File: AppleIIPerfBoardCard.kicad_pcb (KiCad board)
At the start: 2 copper layers, 177.8 x 77.5 mm, 1770 parts, among them J1 Conn_02x25_Counter_Clockwise, J2 50_POS_Card_Edge_Connector

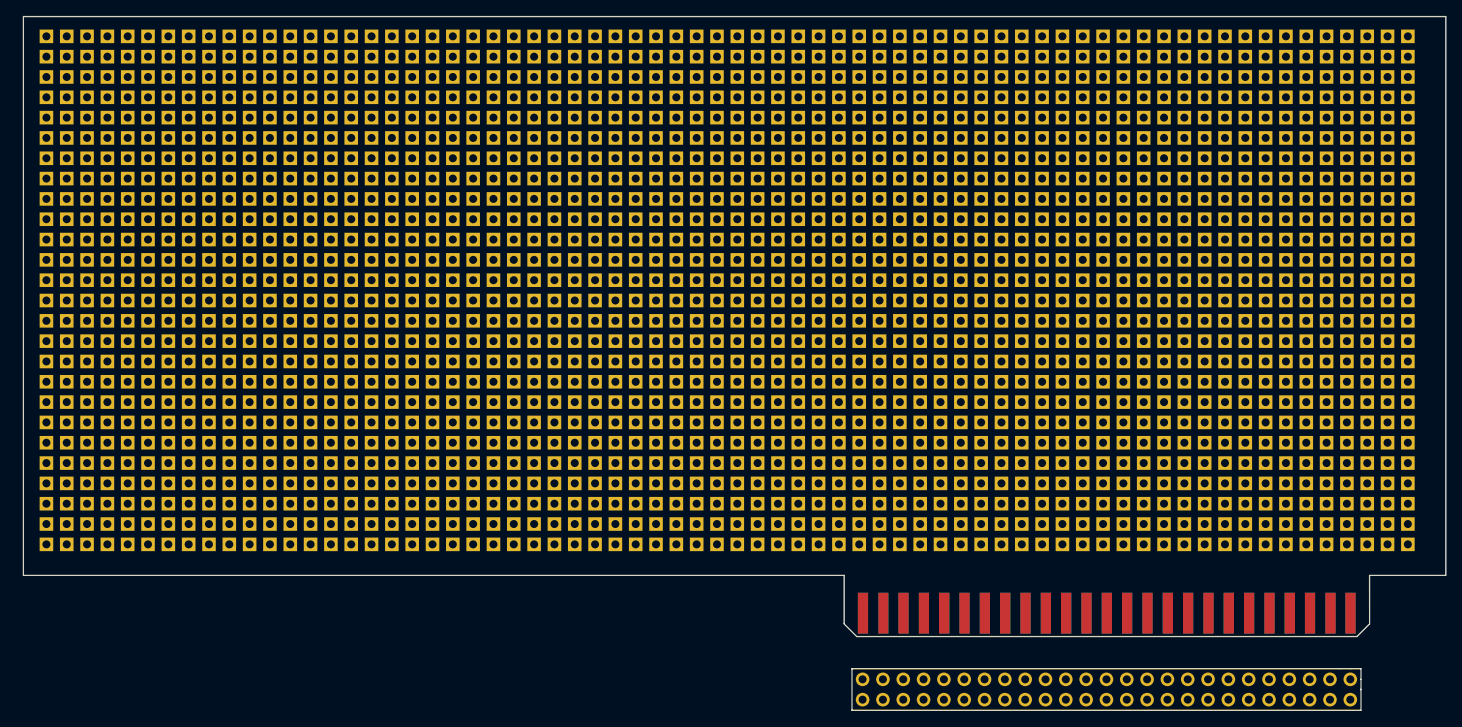
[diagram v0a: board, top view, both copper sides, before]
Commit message: refining perf board and edge connector position
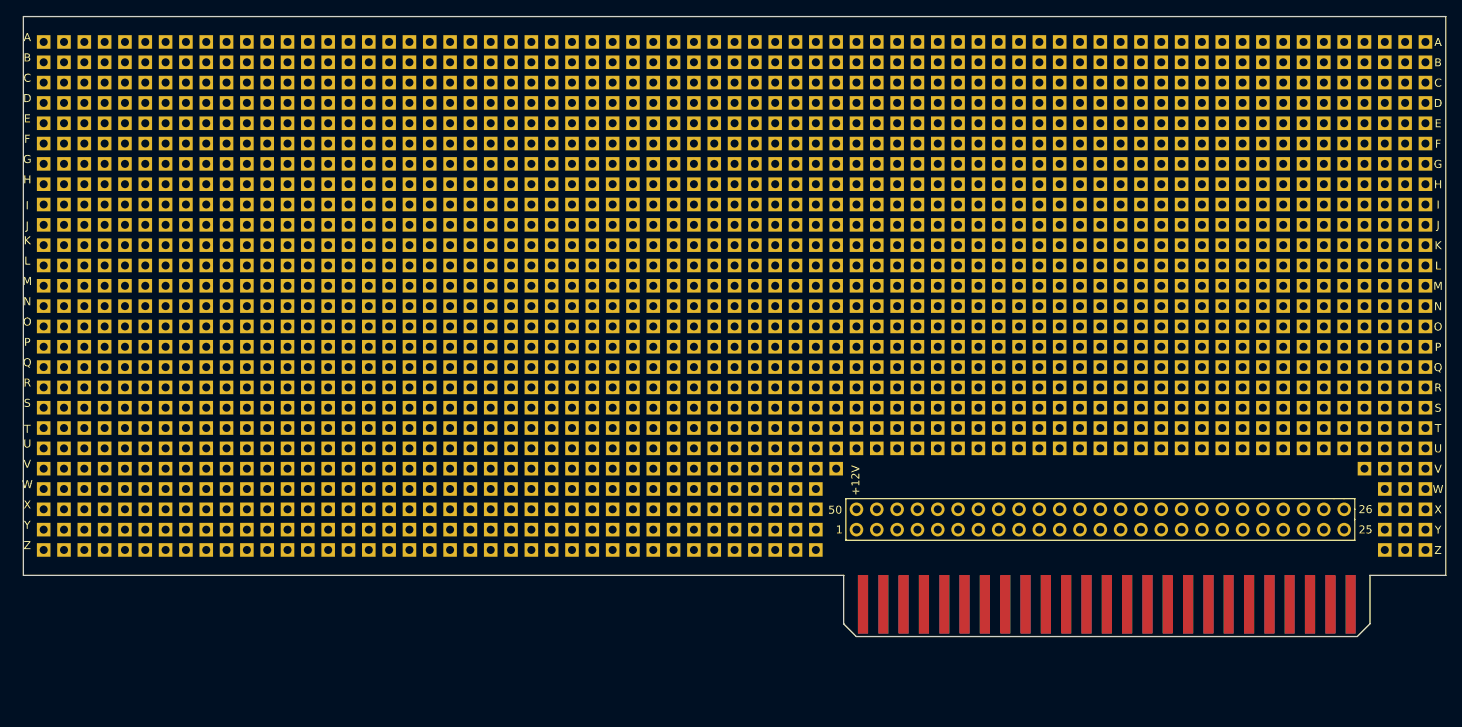
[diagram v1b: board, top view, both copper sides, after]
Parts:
- removed the REF** at (228.1, 126.3)
- removed the REF** at (205.2, 126.3)
- removed the REF** at (149.3, 123.7)
- removed the REF** at (108.7, 90.7)
- removed the REF** at (106.1, 90.7)
- removed the REF** at (103.6, 90.7)
- removed the REF** at (101.1, 90.7)
- removed the REF** at (98.5, 90.7)
- removed the REF** at (96.0, 90.7)
- removed the REF** at (93.4, 90.7)
- removed the REF** at (90.9, 90.7)
- removed the REF** at (88.4, 90.7)
- removed the REF** at (85.8, 90.7)
- removed the REF** at (146.8, 123.7)
- removed the REF** at (83.3, 90.7)
- removed the REF** at (80.7, 90.7)
- removed the REF** at (78.2, 90.7)
- removed the REF** at (75.7, 90.7)
- removed the REF** at (73.1, 90.7)
- removed the REF** at (70.6, 90.7)
- removed the REF** at (68.0, 90.7)
- removed the REF** at (65.5, 90.7)
- removed the REF** at (63.0, 90.7)
- removed the REF** at (60.4, 90.7)
- removed the REF** at (144.2, 123.7)
- removed the REF** at (57.9, 90.7)
- removed the REF** at (228.1, 88.2)
- removed the REF** at (225.5, 88.2)
- removed the REF** at (223.0, 88.2)
- removed the REF** at (220.4, 88.2)
- removed the REF** at (217.9, 88.2)
- removed the REF** at (215.4, 88.2)
- removed the REF** at (212.8, 88.2)
- removed the REF** at (210.3, 88.2)
- removed the REF** at (207.7, 88.2)
- removed the REF** at (141.7, 123.7)
- removed the REF** at (205.2, 88.2)
- removed the REF** at (202.7, 88.2)
- removed the REF** at (200.1, 88.2)
- removed the REF** at (197.6, 88.2)
- removed the REF** at (195.0, 88.2)
- removed the REF** at (192.5, 88.2)
- removed the REF** at (190.0, 88.2)
- removed the REF** at (187.4, 88.2)
- removed the REF** at (184.9, 88.2)
- removed the REF** at (182.3, 88.2)
- removed the REF** at (139.2, 123.7)
- removed the REF** at (179.8, 88.2)
- removed the REF** at (177.3, 88.2)
- removed the REF** at (174.7, 88.2)
- removed the REF** at (172.2, 88.2)
- removed the REF** at (169.6, 88.2)
- removed the REF** at (167.1, 88.2)
- removed the REF** at (164.6, 88.2)
- removed the REF** at (162.0, 88.2)
- removed the REF** at (159.5, 88.2)
- removed the REF** at (156.9, 88.2)
- removed the REF** at (136.6, 123.7)
- removed the REF** at (154.4, 88.2)
- removed the REF** at (151.9, 88.2)
- removed the REF** at (149.3, 88.2)
- removed the REF** at (146.8, 88.2)
- removed the REF** at (144.2, 88.2)
- removed the REF** at (141.7, 88.2)
- removed the REF** at (139.2, 88.2)
- removed the REF** at (136.6, 88.2)
- removed the REF** at (134.1, 88.2)
- removed the REF** at (131.5, 88.2)
- removed the REF** at (134.1, 123.7)
- removed the REF** at (129.0, 88.2)
- removed the REF** at (126.5, 88.2)
- removed the REF** at (123.9, 88.2)
- removed the REF** at (121.4, 88.2)
- removed the REF** at (118.8, 88.2)
- removed the REF** at (116.3, 88.2)
- removed the REF** at (113.8, 88.2)
- removed the REF** at (111.2, 88.2)
- removed the REF** at (108.7, 88.2)
- removed the REF** at (106.1, 88.2)
- removed the REF** at (131.5, 123.7)
- removed the REF** at (103.6, 88.2)
- removed the REF** at (101.1, 88.2)
- removed the REF** at (98.5, 88.2)
- removed the REF** at (96.0, 88.2)
- removed the REF** at (93.4, 88.2)
- removed the REF** at (90.9, 88.2)
- removed the REF** at (88.4, 88.2)
- removed the REF** at (85.8, 88.2)
- removed the REF** at (83.3, 88.2)
- removed the REF** at (80.7, 88.2)
- removed the REF** at (129.0, 123.7)
- removed the REF** at (78.2, 88.2)
- removed the REF** at (75.7, 88.2)
- removed the REF** at (73.1, 88.2)
- removed the REF** at (70.6, 88.2)
- removed the REF** at (68.0, 88.2)
- removed the REF** at (65.5, 88.2)
- removed the REF** at (63.0, 88.2)
- removed the REF** at (60.4, 88.2)
- removed the REF** at (57.9, 88.2)
- removed the REF** at (228.1, 85.6)
- removed the REF** at (126.5, 123.7)
- removed the REF** at (225.5, 85.6)
- removed the REF** at (223.0, 85.6)
- removed the REF** at (220.4, 85.6)
- removed the REF** at (217.9, 85.6)
- removed the REF** at (215.4, 85.6)
- removed the REF** at (212.8, 85.6)
- removed the REF** at (210.3, 85.6)
- removed the REF** at (207.7, 85.6)
- removed the REF** at (205.2, 85.6)
- removed the REF** at (202.7, 85.6)
- removed the REF** at (202.7, 126.3)
- removed the REF** at (123.9, 123.7)
- removed the REF** at (200.1, 85.6)
- removed the REF** at (197.6, 85.6)
- removed the REF** at (195.0, 85.6)
- removed the REF** at (192.5, 85.6)
- removed the REF** at (190.0, 85.6)
- removed the REF** at (187.4, 85.6)
- removed the REF** at (184.9, 85.6)
- removed the REF** at (182.3, 85.6)
- removed the REF** at (179.8, 85.6)
- removed the REF** at (177.3, 85.6)
- removed the REF** at (121.4, 123.7)
- removed the REF** at (174.7, 85.6)
- removed the REF** at (172.2, 85.6)
- removed the REF** at (169.6, 85.6)
- removed the REF** at (167.1, 85.6)
- removed the REF** at (164.6, 85.6)
- removed the REF** at (162.0, 85.6)
- removed the REF** at (159.5, 85.6)
- removed the REF** at (156.9, 85.6)
- removed the REF** at (154.4, 85.6)
- removed the REF** at (151.9, 85.6)
- removed the REF** at (118.8, 123.7)
- removed the REF** at (149.3, 85.6)
- removed the REF** at (146.8, 85.6)
- removed the REF** at (144.2, 85.6)
- removed the REF** at (141.7, 85.6)
- removed the REF** at (139.2, 85.6)
- removed the REF** at (136.6, 85.6)
- removed the REF** at (134.1, 85.6)
- removed the REF** at (131.5, 85.6)
- removed the REF** at (129.0, 85.6)
- removed the REF** at (126.5, 85.6)
- removed the REF** at (116.3, 123.7)
- removed the REF** at (123.9, 85.6)
- removed the REF** at (121.4, 85.6)
- removed the REF** at (118.8, 85.6)
- removed the REF** at (116.3, 85.6)
- removed the REF** at (113.8, 85.6)
- removed the REF** at (111.2, 85.6)
- removed the REF** at (108.7, 85.6)
- removed the REF** at (106.1, 85.6)
- removed the REF** at (103.6, 85.6)
- removed the REF** at (101.1, 85.6)
- removed the REF** at (113.8, 123.7)
- removed the REF** at (98.5, 85.6)
- removed the REF** at (96.0, 85.6)
- removed the REF** at (93.4, 85.6)
- removed the REF** at (90.9, 85.6)
- removed the REF** at (88.4, 85.6)
- removed the REF** at (85.8, 85.6)
- removed the REF** at (83.3, 85.6)
- removed the REF** at (80.7, 85.6)
- removed the REF** at (78.2, 85.6)
- removed the REF** at (75.7, 85.6)
- removed the REF** at (111.2, 123.7)
- removed the REF** at (73.1, 85.6)
- removed the REF** at (70.6, 85.6)
- removed the REF** at (68.0, 85.6)
- removed the REF** at (65.5, 85.6)
- removed the REF** at (63.0, 85.6)
- removed the REF** at (60.4, 85.6)
- removed the REF** at (57.9, 85.6)
- removed the REF** at (228.1, 83.1)
- removed the REF** at (225.5, 83.1)
- removed the REF** at (223.0, 83.1)
- removed the REF** at (108.7, 123.7)
- removed the REF** at (220.4, 83.1)
- removed the REF** at (217.9, 83.1)
- removed the REF** at (215.4, 83.1)
- removed the REF** at (212.8, 83.1)
- removed the REF** at (210.3, 83.1)
- removed the REF** at (207.7, 83.1)
- removed the REF** at (205.2, 83.1)
- removed the REF** at (202.7, 83.1)
- removed the REF** at (200.1, 83.1)
- removed the REF** at (197.6, 83.1)
- removed the REF** at (106.1, 123.7)
- removed the REF** at (195.0, 83.1)
- removed the REF** at (192.5, 83.1)
- removed the REF** at (190.0, 83.1)
- removed the REF** at (187.4, 83.1)
- removed the REF** at (184.9, 83.1)
- removed the REF** at (182.3, 83.1)
- removed the REF** at (179.8, 83.1)
- removed the REF** at (177.3, 83.1)
- removed the REF** at (174.7, 83.1)
- removed the REF** at (172.2, 83.1)
- removed the REF** at (103.6, 123.7)
- removed the REF** at (169.6, 83.1)
- removed the REF** at (167.1, 83.1)
- removed the REF** at (164.6, 83.1)
- removed the REF** at (162.0, 83.1)
- removed the REF** at (159.5, 83.1)
- removed the REF** at (156.9, 83.1)
- removed the REF** at (154.4, 83.1)
- removed the REF** at (151.9, 83.1)
- removed the REF** at (149.3, 83.1)
- removed the REF** at (146.8, 83.1)
- removed the REF** at (101.1, 123.7)
- removed the REF** at (144.2, 83.1)
- removed the REF** at (141.7, 83.1)
- removed the REF** at (139.2, 83.1)
- removed the REF** at (136.6, 83.1)
- removed the REF** at (134.1, 83.1)
- removed the REF** at (131.5, 83.1)
- removed the REF** at (129.0, 83.1)
- removed the REF** at (126.5, 83.1)
- removed the REF** at (123.9, 83.1)
- removed the REF** at (121.4, 83.1)
- removed the REF** at (200.1, 126.3)
- removed the REF** at (98.5, 123.7)
- removed the REF** at (118.8, 83.1)
- removed the REF** at (116.3, 83.1)
- removed the REF** at (113.8, 83.1)
- removed the REF** at (111.2, 83.1)
- removed the REF** at (108.7, 83.1)
- removed the REF** at (106.1, 83.1)
- removed the REF** at (103.6, 83.1)
- removed the REF** at (101.1, 83.1)
- removed the REF** at (98.5, 83.1)
- removed the REF** at (96.0, 83.1)
- removed the REF** at (96.0, 123.7)
- removed the REF** at (93.4, 83.1)
- removed the REF** at (90.9, 83.1)
- removed the REF** at (88.4, 83.1)
- removed the REF** at (85.8, 83.1)
- removed the REF** at (83.3, 83.1)
- removed the REF** at (80.7, 83.1)
- removed the REF** at (78.2, 83.1)
- removed the REF** at (75.7, 83.1)
- removed the REF** at (73.1, 83.1)
- removed the REF** at (70.6, 83.1)
- removed the REF** at (93.4, 123.7)
- removed the REF** at (68.0, 83.1)
- removed the REF** at (65.5, 83.1)
- removed the REF** at (63.0, 83.1)
- removed the REF** at (60.4, 83.1)
- removed the REF** at (57.9, 83.1)
- removed the REF** at (228.1, 80.6)
- removed the REF** at (225.5, 80.6)
- removed the REF** at (223.0, 80.6)
- removed the REF** at (220.4, 80.6)
- removed the REF** at (217.9, 80.6)
- removed the REF** at (90.9, 123.7)
- removed the REF** at (215.4, 80.6)
- removed the REF** at (212.8, 80.6)
- removed the REF** at (210.3, 80.6)
- removed the REF** at (207.7, 80.6)
- removed the REF** at (205.2, 80.6)
- removed the REF** at (202.7, 80.6)
- removed the REF** at (200.1, 80.6)
- removed the REF** at (197.6, 80.6)
- removed the REF** at (195.0, 80.6)
- removed the REF** at (192.5, 80.6)
- removed the REF** at (88.4, 123.7)
- removed the REF** at (190.0, 80.6)
- removed the REF** at (187.4, 80.6)
- removed the REF** at (184.9, 80.6)
- removed the REF** at (182.3, 80.6)
- removed the REF** at (179.8, 80.6)
- removed the REF** at (177.3, 80.6)
- removed the REF** at (174.7, 80.6)
- removed the REF** at (172.2, 80.6)
- removed the REF** at (169.6, 80.6)
- removed the REF** at (167.1, 80.6)
- removed the REF** at (85.8, 123.7)
- removed the REF** at (164.6, 80.6)
- removed the REF** at (162.0, 80.6)
- removed the REF** at (159.5, 80.6)
- removed the REF** at (156.9, 80.6)
- removed the REF** at (154.4, 80.6)
- removed the REF** at (151.9, 80.6)
- removed the REF** at (149.3, 80.6)
- removed the REF** at (146.8, 80.6)
- removed the REF** at (144.2, 80.6)
- removed the REF** at (141.7, 80.6)
- removed the REF** at (83.3, 123.7)
- removed the REF** at (139.2, 80.6)
- removed the REF** at (136.6, 80.6)
- removed the REF** at (134.1, 80.6)
- removed the REF** at (131.5, 80.6)
- removed the REF** at (129.0, 80.6)
- removed the REF** at (126.5, 80.6)
- removed the REF** at (123.9, 80.6)
- removed the REF** at (121.4, 80.6)
- removed the REF** at (118.8, 80.6)
- removed the REF** at (116.3, 80.6)
- removed the REF** at (80.7, 123.7)
- removed the REF** at (113.8, 80.6)
- removed the REF** at (111.2, 80.6)
- removed the REF** at (108.7, 80.6)
- removed the REF** at (106.1, 80.6)
- removed the REF** at (103.6, 80.6)
- removed the REF** at (101.1, 80.6)
- removed the REF** at (98.5, 80.6)
- removed the REF** at (96.0, 80.6)
- removed the REF** at (93.4, 80.6)
- removed the REF** at (90.9, 80.6)
- removed the REF** at (78.2, 123.7)
- removed the REF** at (88.4, 80.6)
- removed the REF** at (85.8, 80.6)
- removed the REF** at (83.3, 80.6)
- removed the REF** at (80.7, 80.6)
- removed the REF** at (78.2, 80.6)
- removed the REF** at (75.7, 80.6)
- removed the REF** at (73.1, 80.6)
- removed the REF** at (70.6, 80.6)
- removed the REF** at (68.0, 80.6)
- removed the REF** at (65.5, 80.6)
- removed the REF** at (75.7, 123.7)
- removed the REF** at (63.0, 80.6)
- removed the REF** at (60.4, 80.6)
- removed the REF** at (57.9, 80.6)
- removed the REF** at (228.1, 78.0)
- removed the REF** at (225.5, 78.0)
- removed the REF** at (223.0, 78.0)
- removed the REF** at (220.4, 78.0)
- removed the REF** at (217.9, 78.0)
- removed the REF** at (215.4, 78.0)
- removed the REF** at (212.8, 78.0)
- removed the REF** at (197.6, 126.3)
- removed the REF** at (73.1, 123.7)
- removed the REF** at (210.3, 78.0)
- removed the REF** at (207.7, 78.0)
- removed the REF** at (205.2, 78.0)
- removed the REF** at (202.7, 78.0)
- removed the REF** at (200.1, 78.0)
- removed the REF** at (197.6, 78.0)
- removed the REF** at (195.0, 78.0)
- removed the REF** at (192.5, 78.0)
- removed the REF** at (190.0, 78.0)
- removed the REF** at (187.4, 78.0)
- removed the REF** at (70.6, 123.7)
- removed the REF** at (184.9, 78.0)
- removed the REF** at (182.3, 78.0)
- removed the REF** at (179.8, 78.0)
- removed the REF** at (177.3, 78.0)
- removed the REF** at (174.7, 78.0)
- removed the REF** at (172.2, 78.0)
- removed the REF** at (169.6, 78.0)
- removed the REF** at (167.1, 78.0)
- removed the REF** at (164.6, 78.0)
- removed the REF** at (162.0, 78.0)
- removed the REF** at (68.0, 123.7)
- removed the REF** at (159.5, 78.0)
- removed the REF** at (156.9, 78.0)
- removed the REF** at (154.4, 78.0)
- removed the REF** at (151.9, 78.0)
- removed the REF** at (149.3, 78.0)
- removed the REF** at (146.8, 78.0)
- removed the REF** at (144.2, 78.0)
- removed the REF** at (141.7, 78.0)
- removed the REF** at (139.2, 78.0)
- removed the REF** at (136.6, 78.0)
- removed the REF** at (65.5, 123.7)
- removed the REF** at (134.1, 78.0)
- removed the REF** at (131.5, 78.0)
- removed the REF** at (129.0, 78.0)
- removed the REF** at (126.5, 78.0)
- removed the REF** at (123.9, 78.0)
- removed the REF** at (121.4, 78.0)
- removed the REF** at (118.8, 78.0)
- removed the REF** at (116.3, 78.0)
- removed the REF** at (113.8, 78.0)
- removed the REF** at (111.2, 78.0)
- removed the REF** at (63.0, 123.7)
- removed the REF** at (108.7, 78.0)
- removed the REF** at (106.1, 78.0)
- removed the REF** at (103.6, 78.0)
- removed the REF** at (101.1, 78.0)
- removed the REF** at (98.5, 78.0)
- removed the REF** at (96.0, 78.0)
- removed the REF** at (93.4, 78.0)
- removed the REF** at (90.9, 78.0)
- removed the REF** at (88.4, 78.0)
- removed the REF** at (85.8, 78.0)
- removed the REF** at (60.4, 123.7)
- removed the REF** at (83.3, 78.0)
- removed the REF** at (80.7, 78.0)
- removed the REF** at (78.2, 78.0)
- removed the REF** at (75.7, 78.0)
- removed the REF** at (73.1, 78.0)
- removed the REF** at (70.6, 78.0)
- removed the REF** at (68.0, 78.0)
- removed the REF** at (65.5, 78.0)
- removed the REF** at (63.0, 78.0)
- removed the REF** at (60.4, 78.0)
- removed the REF** at (57.9, 123.7)
- removed the REF** at (57.9, 78.0)
- removed the REF** at (228.1, 75.5)
- removed the REF** at (225.5, 75.5)
- removed the REF** at (223.0, 75.5)
- removed the REF** at (220.4, 75.5)
- removed the REF** at (217.9, 75.5)
- removed the REF** at (215.4, 75.5)
- removed the REF** at (212.8, 75.5)
- removed the REF** at (210.3, 75.5)
- removed the REF** at (207.7, 75.5)
- removed the REF** at (228.1, 121.2)
- removed the REF** at (205.2, 75.5)
- removed the REF** at (202.7, 75.5)
- removed the REF** at (200.1, 75.5)
- removed the REF** at (197.6, 75.5)
- removed the REF** at (195.0, 75.5)
- removed the REF** at (192.5, 75.5)
- removed the REF** at (190.0, 75.5)
- removed the REF** at (187.4, 75.5)
- removed the REF** at (184.9, 75.5)
- removed the REF** at (182.3, 75.5)
- removed the REF** at (225.5, 121.2)
- removed the REF** at (179.8, 75.5)
- removed the REF** at (177.3, 75.5)
- removed the REF** at (174.7, 75.5)
- removed the REF** at (172.2, 75.5)
- removed the REF** at (169.6, 75.5)
- removed the REF** at (167.1, 75.5)
- removed the REF** at (164.6, 75.5)
- removed the REF** at (162.0, 75.5)
- removed the REF** at (159.5, 75.5)
- removed the REF** at (156.9, 75.5)
- removed the REF** at (223.0, 121.2)
- removed the REF** at (154.4, 75.5)
- removed the REF** at (151.9, 75.5)
- removed the REF** at (149.3, 75.5)
- removed the REF** at (146.8, 75.5)
- removed the REF** at (144.2, 75.5)
- removed the REF** at (141.7, 75.5)
- removed the REF** at (139.2, 75.5)
- removed the REF** at (136.6, 75.5)
- removed the REF** at (134.1, 75.5)
- removed the REF** at (131.5, 75.5)
- removed the REF** at (195.0, 126.3)
- removed the REF** at (220.4, 121.2)
- removed the REF** at (129.0, 75.5)
- removed the REF** at (126.5, 75.5)
- removed the REF** at (123.9, 75.5)
- removed the REF** at (121.4, 75.5)
- removed the REF** at (118.8, 75.5)
- removed the REF** at (116.3, 75.5)
- removed the REF** at (113.8, 75.5)
- removed the REF** at (111.2, 75.5)
- removed the REF** at (108.7, 75.5)
- removed the REF** at (106.1, 75.5)
- removed the REF** at (217.9, 121.2)
- removed the REF** at (103.6, 75.5)
- removed the REF** at (101.1, 75.5)
- removed the REF** at (98.5, 75.5)
- removed the REF** at (96.0, 75.5)
- removed the REF** at (93.4, 75.5)
- removed the REF** at (90.9, 75.5)
- removed the REF** at (88.4, 75.5)
- removed the REF** at (85.8, 75.5)
- removed the REF** at (83.3, 75.5)
- removed the REF** at (80.7, 75.5)
- removed the REF** at (215.4, 121.2)
- removed the REF** at (78.2, 75.5)
- removed the REF** at (75.7, 75.5)
- removed the REF** at (73.1, 75.5)
- removed the REF** at (70.6, 75.5)
- removed the REF** at (68.0, 75.5)
- removed the REF** at (65.5, 75.5)
- removed the REF** at (63.0, 75.5)
- removed the REF** at (60.4, 75.5)
- removed the REF** at (57.9, 75.5)
- removed the REF** at (228.1, 72.9)
- removed the REF** at (212.8, 121.2)
- removed the REF** at (225.5, 72.9)
- removed the REF** at (223.0, 72.9)
- removed the REF** at (220.4, 72.9)
- removed the REF** at (217.9, 72.9)
- removed the REF** at (215.4, 72.9)
- removed the REF** at (212.8, 72.9)
- removed the REF** at (210.3, 72.9)
- removed the REF** at (207.7, 72.9)
- removed the REF** at (205.2, 72.9)
- removed the REF** at (202.7, 72.9)
- removed the REF** at (210.3, 121.2)
- removed the REF** at (200.1, 72.9)
- removed the REF** at (197.6, 72.9)
- removed the REF** at (195.0, 72.9)
- removed the REF** at (192.5, 72.9)
- removed the REF** at (190.0, 72.9)
- removed the REF** at (187.4, 72.9)
- removed the REF** at (184.9, 72.9)
- removed the REF** at (182.3, 72.9)
- removed the REF** at (179.8, 72.9)
- removed the REF** at (177.3, 72.9)
- removed the REF** at (207.7, 121.2)
- removed the REF** at (174.7, 72.9)
- removed the REF** at (172.2, 72.9)
- removed the REF** at (169.6, 72.9)
- removed the REF** at (167.1, 72.9)
- removed the REF** at (164.6, 72.9)
- removed the REF** at (162.0, 72.9)
- removed the REF** at (159.5, 72.9)
- removed the REF** at (156.9, 72.9)
- removed the REF** at (154.4, 72.9)
- removed the REF** at (151.9, 72.9)
- removed the REF** at (205.2, 121.2)
- removed the REF** at (149.3, 72.9)
- removed the REF** at (146.8, 72.9)
- removed the REF** at (144.2, 72.9)
- removed the REF** at (141.7, 72.9)
- removed the REF** at (139.2, 72.9)
- removed the REF** at (136.6, 72.9)
- removed the REF** at (134.1, 72.9)
- removed the REF** at (131.5, 72.9)
- removed the REF** at (129.0, 72.9)
- removed the REF** at (126.5, 72.9)
- removed the REF** at (202.7, 121.2)
- removed the REF** at (123.9, 72.9)
- removed the REF** at (121.4, 72.9)
- removed the REF** at (118.8, 72.9)
- removed the REF** at (116.3, 72.9)
- removed the REF** at (113.8, 72.9)
- removed the REF** at (111.2, 72.9)
- removed the REF** at (108.7, 72.9)
- removed the REF** at (106.1, 72.9)
- removed the REF** at (103.6, 72.9)
- removed the REF** at (101.1, 72.9)
- removed the REF** at (200.1, 121.2)
- removed the REF** at (98.5, 72.9)
- removed the REF** at (96.0, 72.9)
- removed the REF** at (93.4, 72.9)
- removed the REF** at (90.9, 72.9)
- removed the REF** at (88.4, 72.9)
- removed the REF** at (85.8, 72.9)
- removed the REF** at (83.3, 72.9)
- removed the REF** at (80.7, 72.9)
- removed the REF** at (78.2, 72.9)
- removed the REF** at (75.7, 72.9)
- removed the REF** at (197.6, 121.2)
- removed the REF** at (73.1, 72.9)
- removed the REF** at (70.6, 72.9)
- removed the REF** at (68.0, 72.9)
- removed the REF** at (65.5, 72.9)
- removed the REF** at (63.0, 72.9)
- removed the REF** at (60.4, 72.9)
- removed the REF** at (57.9, 72.9)
- removed the REF** at (228.1, 70.4)
- removed the REF** at (225.5, 70.4)
- removed the REF** at (223.0, 70.4)
- removed the REF** at (192.5, 126.3)
- removed the REF** at (195.0, 121.2)
- removed the REF** at (220.4, 70.4)
- removed the REF** at (217.9, 70.4)
- removed the REF** at (215.4, 70.4)
- removed the REF** at (212.8, 70.4)
- removed the REF** at (210.3, 70.4)
- removed the REF** at (207.7, 70.4)
- removed the REF** at (205.2, 70.4)
- removed the REF** at (202.7, 70.4)
- removed the REF** at (200.1, 70.4)
- removed the REF** at (197.6, 70.4)
- removed the REF** at (192.5, 121.2)
- removed the REF** at (195.0, 70.4)
- removed the REF** at (192.5, 70.4)
- removed the REF** at (190.0, 70.4)
- removed the REF** at (187.4, 70.4)
- removed the REF** at (184.9, 70.4)
- removed the REF** at (182.3, 70.4)
- removed the REF** at (179.8, 70.4)
- removed the REF** at (177.3, 70.4)
- removed the REF** at (174.7, 70.4)
- removed the REF** at (172.2, 70.4)
- removed the REF** at (190.0, 121.2)
- removed the REF** at (169.6, 70.4)
- removed the REF** at (167.1, 70.4)
- removed the REF** at (164.6, 70.4)
- removed the REF** at (162.0, 70.4)
- removed the REF** at (159.5, 70.4)
- removed the REF** at (156.9, 70.4)
- removed the REF** at (154.4, 70.4)
- removed the REF** at (151.9, 70.4)
- removed the REF** at (149.3, 70.4)
- removed the REF** at (146.8, 70.4)
- removed the REF** at (187.4, 121.2)
- removed the REF** at (144.2, 70.4)
- removed the REF** at (141.7, 70.4)
- removed the REF** at (139.2, 70.4)
- removed the REF** at (136.6, 70.4)
- removed the REF** at (134.1, 70.4)
- removed the REF** at (131.5, 70.4)
- removed the REF** at (129.0, 70.4)
- removed the REF** at (126.5, 70.4)
- removed the REF** at (123.9, 70.4)
- removed the REF** at (121.4, 70.4)
- removed the REF** at (184.9, 121.2)
- removed the REF** at (118.8, 70.4)
- removed the REF** at (116.3, 70.4)
- removed the REF** at (113.8, 70.4)
- removed the REF** at (111.2, 70.4)
- removed the REF** at (108.7, 70.4)
- removed the REF** at (106.1, 70.4)
- removed the REF** at (103.6, 70.4)
- removed the REF** at (101.1, 70.4)
- removed the REF** at (98.5, 70.4)
- removed the REF** at (96.0, 70.4)
- removed the REF** at (182.3, 121.2)
- removed the REF** at (93.4, 70.4)
- removed the REF** at (90.9, 70.4)
- removed the REF** at (88.4, 70.4)
- removed the REF** at (85.8, 70.4)
- removed the REF** at (83.3, 70.4)
- removed the REF** at (80.7, 70.4)
- removed the REF** at (78.2, 70.4)
- removed the REF** at (75.7, 70.4)
- removed the REF** at (73.1, 70.4)
- removed the REF** at (70.6, 70.4)
- removed the REF** at (179.8, 121.2)
- removed the REF** at (68.0, 70.4)
- removed the REF** at (65.5, 70.4)
- removed the REF** at (63.0, 70.4)
- removed the REF** at (60.4, 70.4)
- removed the REF** at (57.9, 70.4)
- removed the REF** at (228.1, 67.9)
- removed the REF** at (225.5, 67.9)
- removed the REF** at (223.0, 67.9)
- removed the REF** at (220.4, 67.9)
- removed the REF** at (217.9, 67.9)
- removed the REF** at (177.3, 121.2)
- removed the REF** at (215.4, 67.9)
- removed the REF** at (212.8, 67.9)
- removed the REF** at (210.3, 67.9)
- removed the REF** at (207.7, 67.9)
- removed the REF** at (205.2, 67.9)
- removed the REF** at (202.7, 67.9)
- removed the REF** at (200.1, 67.9)
- removed the REF** at (197.6, 67.9)
- removed the REF** at (195.0, 67.9)
- removed the REF** at (192.5, 67.9)
- removed the REF** at (174.7, 121.2)
- removed the REF** at (190.0, 67.9)
- removed the REF** at (187.4, 67.9)
- removed the REF** at (184.9, 67.9)
- removed the REF** at (182.3, 67.9)
- removed the REF** at (179.8, 67.9)
- removed the REF** at (177.3, 67.9)
- removed the REF** at (174.7, 67.9)
- removed the REF** at (172.2, 67.9)
- removed the REF** at (169.6, 67.9)
- removed the REF** at (167.1, 67.9)
- removed the REF** at (172.2, 121.2)
- removed the REF** at (164.6, 67.9)
- removed the REF** at (162.0, 67.9)
- removed the REF** at (159.5, 67.9)
- removed the REF** at (156.9, 67.9)
- removed the REF** at (154.4, 67.9)
- removed the REF** at (151.9, 67.9)
- removed the REF** at (149.3, 67.9)
- removed the REF** at (146.8, 67.9)
- removed the REF** at (144.2, 67.9)
- removed the REF** at (141.7, 67.9)
- removed the REF** at (190.0, 126.3)
- removed the REF** at (169.6, 121.2)
- removed the REF** at (139.2, 67.9)
- removed the REF** at (136.6, 67.9)
- removed the REF** at (134.1, 67.9)
- removed the REF** at (131.5, 67.9)
- removed the REF** at (129.0, 67.9)
- removed the REF** at (126.5, 67.9)
- removed the REF** at (123.9, 67.9)
- removed the REF** at (121.4, 67.9)
- removed the REF** at (118.8, 67.9)
- removed the REF** at (116.3, 67.9)
- removed the REF** at (167.1, 121.2)
- removed the REF** at (113.8, 67.9)
- removed the REF** at (111.2, 67.9)
- removed the REF** at (108.7, 67.9)
- removed the REF** at (106.1, 67.9)
- removed the REF** at (103.6, 67.9)
- removed the REF** at (101.1, 67.9)
- removed the REF** at (98.5, 67.9)
- removed the REF** at (96.0, 67.9)
- removed the REF** at (93.4, 67.9)
- removed the REF** at (90.9, 67.9)
- removed the REF** at (164.6, 121.2)
- removed the REF** at (88.4, 67.9)
- removed the REF** at (85.8, 67.9)
- removed the REF** at (83.3, 67.9)
- removed the REF** at (80.7, 67.9)
- removed the REF** at (78.2, 67.9)
- removed the REF** at (75.7, 67.9)
- removed the REF** at (73.1, 67.9)
- removed the REF** at (70.6, 67.9)
- removed the REF** at (68.0, 67.9)
- removed the REF** at (65.5, 67.9)
- removed the REF** at (162.0, 121.2)
- removed the REF** at (63.0, 67.9)
- removed the REF** at (60.4, 67.9)
- removed the REF** at (57.9, 67.9)
- removed the REF** at (228.1, 65.3)
- removed the REF** at (225.5, 65.3)
- removed the REF** at (223.0, 65.3)
- removed the REF** at (220.4, 65.3)
- removed the REF** at (217.9, 65.3)
- removed the REF** at (215.4, 65.3)
- removed the REF** at (212.8, 65.3)
- removed the REF** at (159.5, 121.2)
- removed the REF** at (210.3, 65.3)
- removed the REF** at (207.7, 65.3)
- removed the REF** at (205.2, 65.3)
- removed the REF** at (202.7, 65.3)
- removed the REF** at (200.1, 65.3)
- removed the REF** at (197.6, 65.3)
- removed the REF** at (195.0, 65.3)
- removed the REF** at (192.5, 65.3)
- removed the REF** at (190.0, 65.3)
- removed the REF** at (187.4, 65.3)
- removed the REF** at (156.9, 121.2)
- removed the REF** at (184.9, 65.3)
- removed the REF** at (182.3, 65.3)
- removed the REF** at (179.8, 65.3)
- removed the REF** at (177.3, 65.3)
- removed the REF** at (174.7, 65.3)
- removed the REF** at (172.2, 65.3)
- removed the REF** at (169.6, 65.3)
- removed the REF** at (167.1, 65.3)
- removed the REF** at (164.6, 65.3)
- removed the REF** at (162.0, 65.3)
- removed the REF** at (154.4, 121.2)
- removed the REF** at (159.5, 65.3)
- removed the REF** at (156.9, 65.3)
- removed the REF** at (154.4, 65.3)
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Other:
- outline, holes or cut-outs redrawn
- board text added: "+12V"
- board text added: "1"
- board text added: "25"
- board text added: "26"
- board text added: "50"
- board text added: "A"
- board text added: "B"
- board text added: "C"
- board text added: "D"
- board text added: "E"
- board text added: "F"
- board text added: "G"
- board text added: "H"
- board text added: "I"
- board text added: "J"
- board text added: "K"
- board text added: "L"
- board text added: "M"
- board text added: "N"
- board text added: "O"
- board text added: "P"
- board text added: "Q"
- board text added: "R"
- board text added: "S"
- board text added: "T"
- board text added: "U"
- board text added: "V"
- board text added: "W"
- board text added: "X"
- board text added: "Y"
- board text added: "Z"

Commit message: routed traces
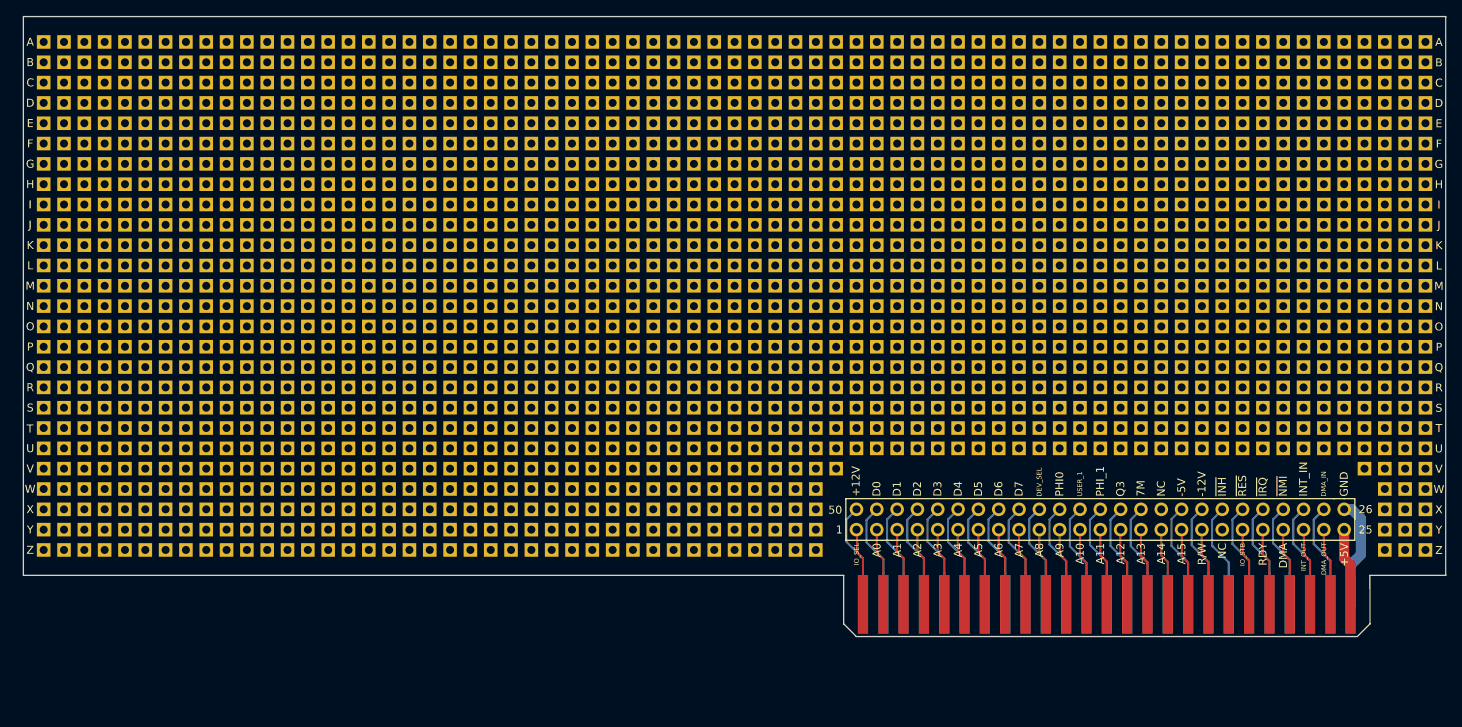
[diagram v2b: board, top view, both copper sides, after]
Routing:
- net /GND: track 0.00 -> 13.8 mm
- net /DMA_IN: track 0.00 -> 13.3 mm
- net /D5: track 0.00 -> 13.3 mm
- net /-12V: track 0.00 -> 13.3 mm
- net /~IRQ: track 0.00 -> 13.3 mm
- net /-5V: track 0.00 -> 13.2 mm
- net /D6: track 0.00 -> 13.2 mm
- net /~NMI: track 0.00 -> 13.2 mm
- net /~RES: track 0.00 -> 13.2 mm
- net /PHI2: track 0.00 -> 13.2 mm
- net /PHI1: track 0.00 -> 13.2 mm
- net /~DEVICE_SELECT: track 0.00 -> 13.2 mm
- net /D7: track 0.00 -> 13.2 mm
- net /~INH: track 0.00 -> 13.2 mm
- net /USER_1: track 0.00 -> 13.2 mm
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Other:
- board text added: "+5V"
- board text added: "-12V"
- board text added: "-5V"
- board text added: "7M"
- board text added: "A0"
- board text added: "A1"
- board text added: "A10"
- board text added: "A11"
- board text added: "A12"
- board text added: "A13"
- board text added: "A14"
- board text added: "A15"
- board text added: "A2"
- board text added: "A3"
- board text added: "A4"
- board text added: "A5"
- board text added: "A6"
- board text added: "A7"
- board text added: "A8"
- board text added: "A9"
- board text added: "D0"
- board text added: "D1"
- board text added: "D2"
- board text added: "D3"
- board text added: "D4"
- board text added: "D5"
- board text added: "D6"
- board text added: "D7"
- board text added: "DEV_SEL"
- board text added: "DMA"
- board text added: "DMA_IN"
- board text added: "DMA_OUT"
- board text added: "GND"
- board text added: "INT_IN"
- board text added: "INT_OUT"
- board text added: "IO_SEL"
- board text added: "IO_STB"
- board text added: "NC"
- board text added: "PHI0"
- board text added: "PHI_1"
- board text added: "Q3"
- board text added: "R/W"
- board text added: "RDY"
- board text added: "USER_1"
- board text added: "~INH"
- board text added: "~IRQ"
- board text added: "~NMI"
- board text added: "~RES"

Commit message: rev1.a release and sent to board fab
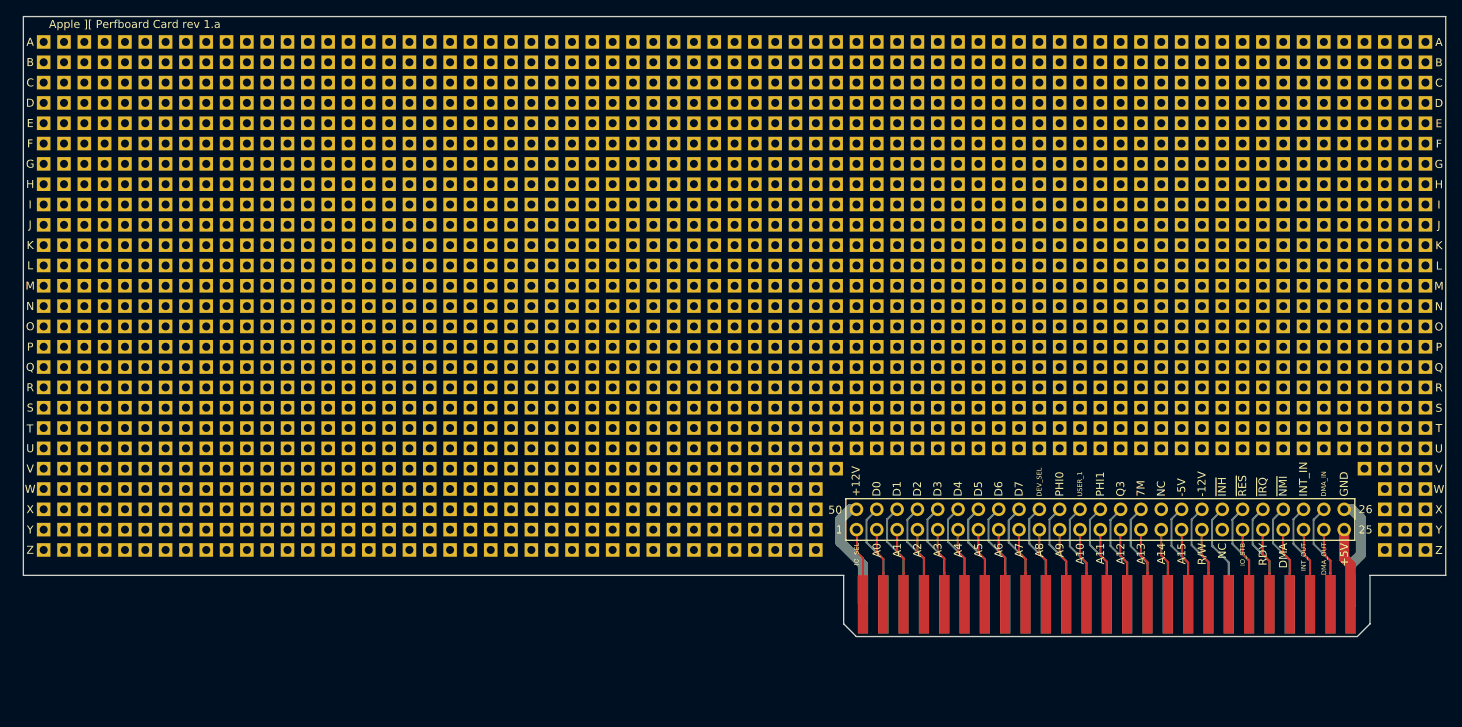
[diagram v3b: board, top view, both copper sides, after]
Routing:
- net /+12V: track 13.2 -> 14.4 mm
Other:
- board text added: "Apple ][ Perfboard Card rev 1.a"
- board text added: "JLCJLCJLCJLC"
- board text added: "PHI1"
- board text removed: "PHI_1"
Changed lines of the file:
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@@
   (general
     (thickness 1.6)
-    (drawings 222)
-    (tracks 244)
+    (drawings 224)
+    (tracks 245)
     (zones 0)
     (modules 1663)
@@
   )
   (setup
-    (last_trace_width 0.254)
+    (last_trace_width 1.27)
     (user_trace_width 0.254)
     (user_trace_width 1.27)
@@
     (visible_elements 7FF9FFFF)
     (pcbplotparams
-      (layerselection 0x010fc_ffffffff)
-      (usegerberextensions false)
+      (layerselection 0x010f0_ffffffff)
+      (usegerberextensions true)
       (usegerberattributes false)
       (usegerberadvancedattributes false)
@@
       (plotinvisibletext false)
       (padsonsilk false)
-      (subtractmaskfromsilk false)
+      (subtractmaskfromsilk true)
       (outputformat 1)
       (mirror false)
-      (drillshape 1)
+      (drillshape 0)
       (scaleselection 1)
-      (outputdirectory ""))
+      (outputdirectory "gerber/"))
   )
   (net 0 "")
@@
     (pad 1 thru_hole rect (at 0 0) (size 1.7 1.7) (drill 1) (layers *.Cu *.Mask))
   )
+  (gr_text JLCJLCJLCJLC (at 214.27186 61.48832) (layer B.SilkS)
+    (effects (font (size 1 1) (thickness 0.15)))
+  )
+  (gr_text "Apple ][ Perfboard Card rev 1.a" (at 68.92036 61.26226) (layer F.SilkS)
+    (effects (font (size 1 1) (thickness 0.15)))
+  )
   (gr_text Z (at 231.92486 126.99238) (layer B.SilkS)
     (effects (font (size 1 1) (thickness 0.15)) (justify mirror))
@@
     (effects (font (size 1 1) (thickness 0.15)) (justify left mirror))
   )
-  (gr_text PHI_1 (at 189.615055 115.89512 90) (layer B.SilkS)
+  (gr_text PHI1 (at 189.59576 116.66474 90) (layer B.SilkS)
     (effects (font (size 1 1) (thickness 0.15)) (justify left mirror))
   )
@@
     (effects (font (size 1 1) (thickness 0.15)) (justify left))
   )
-  (gr_text PHI_1 (at 189.59576 120.30456 90) (layer F.SilkS)
+  (gr_text PHI1 (at 189.59576 120.30456 90) (layer F.SilkS)
     (effects (font (size 1 1) (thickness 0.15)) (justify left))
   )
@@
   (segment (start 162.482341 133.759141) (end 162.482341 129.855141) (width 0.254) (layer B.Cu) (net 49))
   (segment (start 162.482341 129.855141) (end 162.48634 129.851142) (width 0.254) (layer B.Cu) (net 49))
-  (segment (start 157.861 123.18746) (end 159.08782 121.96064) (width 0.254) (layer B.Cu) (net 50))
-  (segment (start 157.861 125.9332) (end 157.861 123.18746) (width 0.254) (layer B.Cu) (net 50))
-  (segment (start 159.942341 133.759141) (end 159.942341 128.014541) (width 0.254) (layer B.Cu) (net 50))
-  (segment (start 159.942341 128.014541) (end 157.861 125.9332) (width 0.254) (layer B.Cu) (net 50))
+  (segment (start 159.942341 128.839141) (end 157.10154 125.99834) (width 1.27) (layer B.Cu) (net 50))
+  (segment (start 159.942341 133.759141) (end 159.942341 128.839141) (width 1.27) (layer B.Cu) (net 50))
+  (segment (start 157.10154 125.99834) (end 157.10154 123.14682) (width 1.27) (layer B.Cu) (net 50))
+  (segment (start 157.10154 123.14682) (end 158.369 121.87936) (width 1.27) (layer B.Cu) (net 50))
+  (segment (start 158.369 121.87936) (end 159.13862 121.87936) (width 1.27) (layer B.Cu) (net 50))
 )
